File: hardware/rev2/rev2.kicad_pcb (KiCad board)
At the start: 4 copper layers, 60 x 40 mm, 109 parts, among them J1 USB_C_Receptacle_USB2.0_16P, J2 uFL, J3 uFL, J4 Antenna RF and GNSS Data, J5 Antenna GND, J6 uFL, Q1 SS8050, SW1 SW_Push, SW2 SW_Push, U1 EClamp2522P, U2 ESP32-S3FN8, U3 SX1262IMLTRT, U4 PE4259, U5 MP2664GG-xxxx-P, U6 MAX17055ETB+, U7 TPS63805YFFR, Y1 ECS-2520SMV-400-FN-TR, Y2 TXO-20CSMV-320

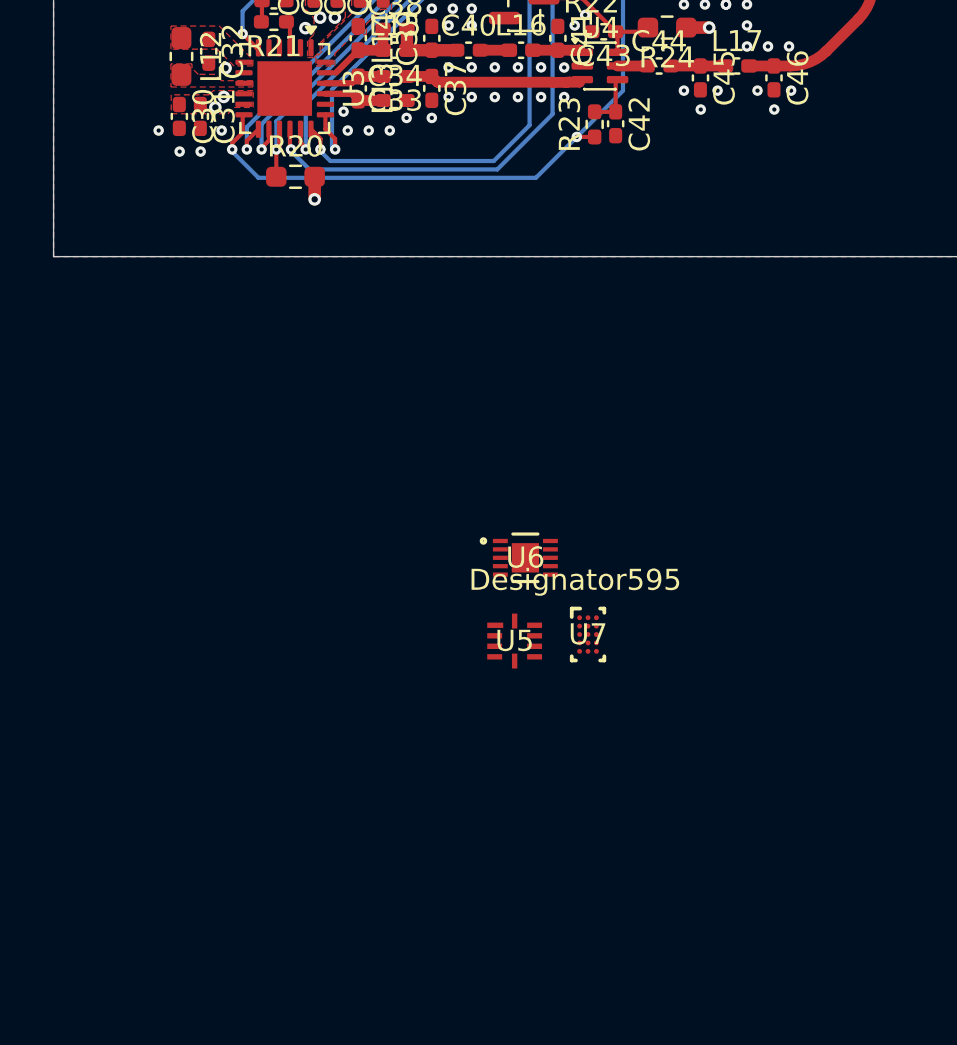
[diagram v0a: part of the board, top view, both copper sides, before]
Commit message: Started power system layout
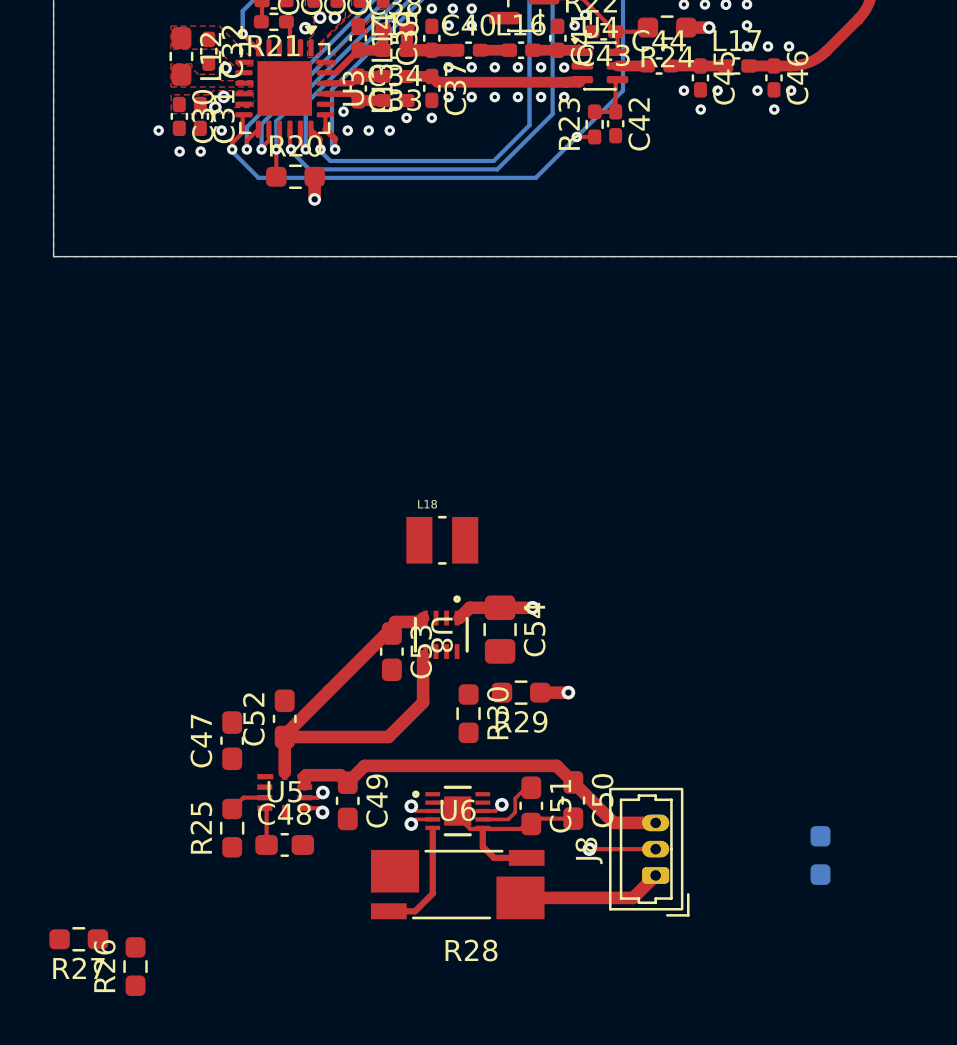
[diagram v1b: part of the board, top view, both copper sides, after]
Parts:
- removed U7: TPS63805YFFR, _footprints:YFF0015AHAN
- added C47: 1µF, Capacitor_SMD:C_0603_1608Metric_Pad1.08x0.95mm_HandSolder, F.Cu at (136.5, 120.0)
- added C48: 100nF, Capacitor_SMD:C_0603_1608Metric_Pad1.08x0.95mm_HandSolder, F.Cu at (139.0, 125.0)
- added C49: 4.7µF, Capacitor_SMD:C_0603_1608Metric_Pad1.08x0.95mm_HandSolder, F.Cu at (142.0, 122.9)
- added C50: 0.1µF, Capacitor_SMD:C_0603_1608Metric_Pad1.08x0.95mm_HandSolder, F.Cu at (152.7, 122.9)
- added C51: 0.47µF, Capacitor_SMD:C_0603_1608Metric_Pad1.08x0.95mm_HandSolder, F.Cu at (150.7, 123.1)
- added C52: 10µF, Capacitor_SMD:C_0603_1608Metric_Pad1.08x0.95mm_HandSolder, F.Cu at (139.0, 119.0)
- added C53: 22µF, Capacitor_SMD:C_0603_1608Metric_Pad1.08x0.95mm_HandSolder, F.Cu at (144.1, 115.8)
- added C54: 47µF, Capacitor_SMD:C_0805_2012Metric_Pad1.18x1.45mm_HandSolder, F.Cu at (149.2, 114.8)
- added J8: Battery Connection, Connector_Molex:Molex_PicoBlade_53047-0310_1x03_P1.25mm_Vertical, F.Cu at (156.7, 126.5)
- added L18: 1µH, _footprints:INDC2520X120N, F.Cu at (146.5, 110.5)
- added R25: 300kΩ, Resistor_SMD:R_0603_1608Metric_Pad0.98x0.95mm_HandSolder, F.Cu at (136.5, 124.2)
- added R26: TBD, Resistor_SMD:R_0603_1608Metric_Pad0.98x0.95mm_HandSolder, F.Cu at (131.9, 130.8)
- added R27: TBD, Resistor_SMD:R_0603_1608Metric_Pad0.98x0.95mm_HandSolder, F.Cu at (129.2, 129.5)
- added R28: 0.01Ω, _footprints:RES_WSK2512R0100FEA, F.Cu at (147.2, 126.9)
- added R29: 511kΩ, Resistor_SMD:R_0603_1608Metric_Pad0.98x0.95mm_HandSolder, F.Cu at (150.2, 117.8)
- added R30: 91kΩ, Resistor_SMD:R_0603_1608Metric_Pad0.98x0.95mm_HandSolder, F.Cu at (147.8, 118.8)
- added R31: TBD, Resistor_SMD:R_0603_1608Metric_Pad0.98x0.95mm_HandSolder, B.Cu at (164.5, 125.5)
- added U8: TPS631000DRLR, _footprints:TPS631000DRLR_TEX, F.Cu at (146.5, 115.0)
- moved U5 13.1 mm to (139.0, 122.5)
- moved U6 12.5 mm to (147.2, 123.4)
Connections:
- net /Power/BATT- renamed /Power/CSP
- U6 pad 5: GND -> /Power/CSN
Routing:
- net Net-(U5-SYS): track 0.00 -> 20.2 mm
- net /Power/BATT+: track 0.00 -> 18.7 mm
- net /Power/CSP: track 0.00 -> 10.7 mm
- net /Power/BATT-: track 0.00 -> 6.88 mm
- net /Power/CSN: track 0.00 -> 5.52 mm
- net +3.3V: track 0.00 -> 5.02 mm, vias 0 -> 2
- net Net-(U6-REG): track 0.00 -> 3.43 mm
- net /Power/NTC: track 0.00 -> 3.16 mm, vias 0 -> 1
- net /RXD/SDA: track 16.8 -> 18.9 mm, vias 1 -> 3
- net /TXD/SCL: track 20.2 -> 22.2 mm, vias 1 -> 3
- net /Power/VDD: track 0.00 -> 1.79 mm
- net /Power/INT: track 0.50 -> 2.27 mm
- net /ESP32/ALRT: track 0.85 -> 1.88 mm, vias 1 -> 2

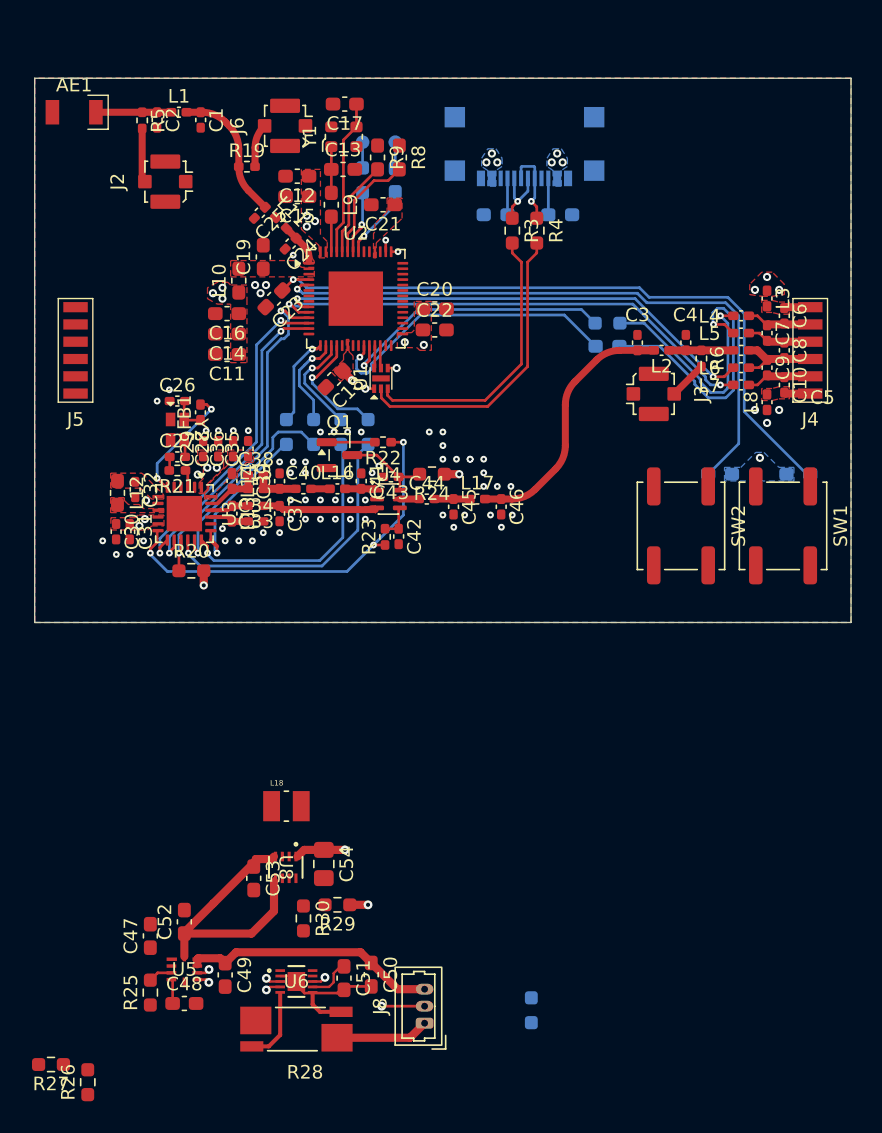
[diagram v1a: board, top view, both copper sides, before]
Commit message: added testpoints, added LEDs, fixed a lot of DRC stuff
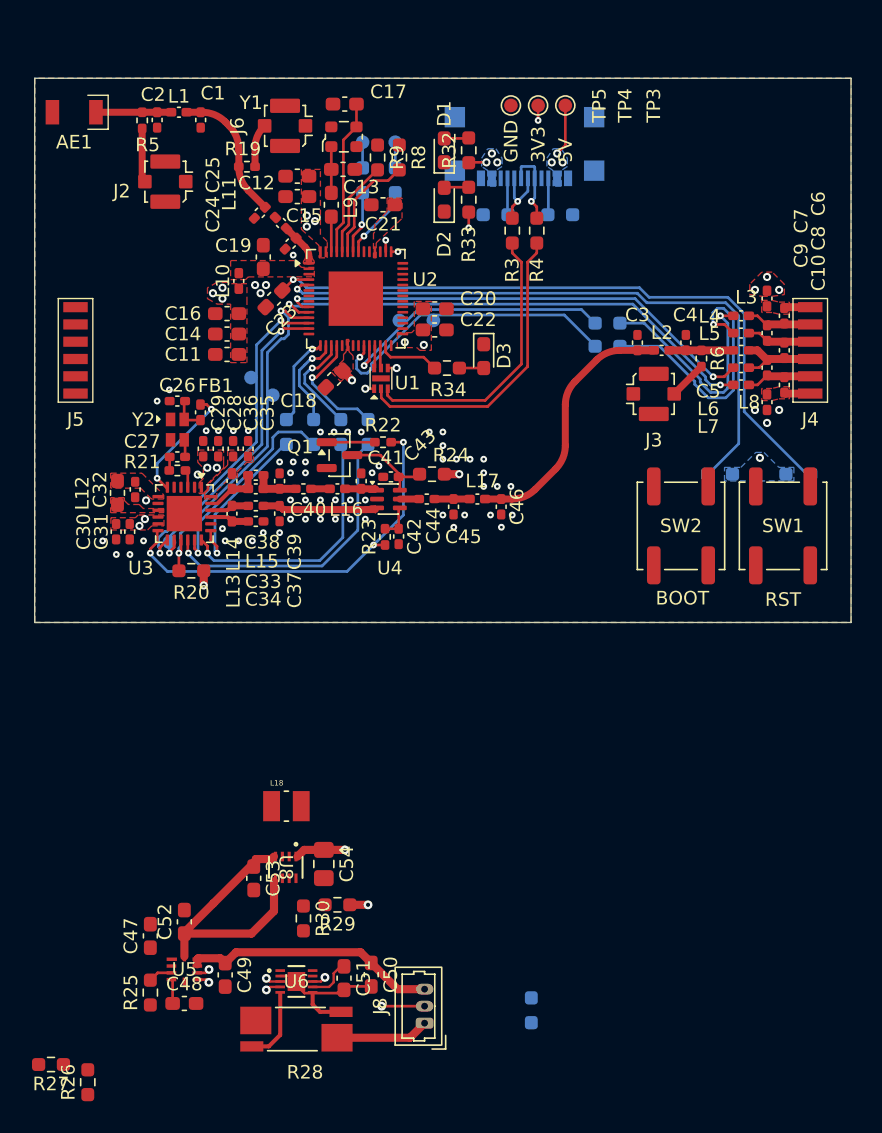
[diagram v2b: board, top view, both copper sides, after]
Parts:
- added D1: LED, LED_SMD:LED_0603_1608Metric_Pad1.05x0.95mm_HandSolder, F.Cu at (158.1, 62.3)
- added D2: LED, LED_SMD:LED_0603_1608Metric_Pad1.05x0.95mm_HandSolder, F.Cu at (158.1, 65.9)
- added D3: LED, LED_SMD:LED_0603_1608Metric_Pad1.05x0.95mm_HandSolder, F.Cu at (161.0, 77.4)
- added R32: 110 R, Resistor_SMD:R_0603_1608Metric_Pad0.98x0.95mm_HandSolder, F.Cu at (159.9, 62.3)
- added R33: 27 R, Resistor_SMD:R_0603_1608Metric_Pad0.98x0.95mm_HandSolder, F.Cu at (159.9, 65.9)
- added R34: 27 R, Resistor_SMD:R_0603_1608Metric_Pad0.98x0.95mm_HandSolder, F.Cu at (158.3, 78.3)
- added TP10: TestPoint, TestPoint:TestPoint_Pad_D1.0mm, B.Cu at (145.5, 80.3)
- added TP11: TestPoint, TestPoint:TestPoint_Pad_D1.0mm, B.Cu at (143.9, 79.0)
- added TP12: TestPoint, TestPoint:TestPoint_Pad_D1.0mm, B.Cu at (137.9, 91.1)
- added TP3: TestPoint, TestPoint:TestPoint_Pad_D1.0mm, F.Cu at (167.0, 59.0)
- added TP4: TestPoint, TestPoint:TestPoint_Pad_D1.0mm, F.Cu at (165.0, 59.0)
- added TP5: TestPoint, TestPoint:TestPoint_Pad_D1.0mm, F.Cu at (163.0, 59.0)
- added TP7: TestPoint, TestPoint:TestPoint_Pad_D1.0mm, B.Cu at (157.3, 74.8)
- added TP8: TestPoint, TestPoint:TestPoint_Pad_D1.0mm, B.Cu at (154.8, 74.8)
- C47: value 1µF -> 1 uF
- C48: value 100nF -> 100 nF
- C49: value 4.7µF -> 4.7 uF
- C5: value DC-Block -> 100 pF
- C50: value 0.1µF -> 0.1 uF
- C51: value 0.47µF -> 0.47 uF
- C52: value 10µF -> 10 uF
- C53: value 22µF -> 22 uF
- C54: value 47µF -> 47 uF
- L10: footprint Inductor_SMD:L_0603_1608Metric_Pad1.05x0.95mm_HandSolder -> Inductor_SMD:L_0402_1005Metric_Pad0.77x0.64mm_HandSolder
- L18: value 1µH -> 1 uH
- R1, R2: value 5.1k -> 5.1 k; footprint Inductor_SMD:L_0603_1608Metric_Pad1.05x0.95mm_HandSolder -> Resistor_SMD:R_0603_1608Metric_Pad0.98x0.95mm_HandSolder
- R10, R7, R8, R9: value 10k -> 10 k; footprint Inductor_SMD:L_0603_1608Metric_Pad1.05x0.95mm_HandSolder -> Resistor_SMD:R_0603_1608Metric_Pad0.98x0.95mm_HandSolder
- R15, R17: footprint Inductor_SMD:L_0603_1608Metric_Pad1.05x0.95mm_HandSolder -> Resistor_SMD:R_0603_1608Metric_Pad0.98x0.95mm_HandSolder
- R20, R24: value 10k -> 10 k
- R25: value 300kΩ -> 300 k
- R28: value 0.01Ω -> 0.01 R
- R29: value 511kΩ -> 511 k
- R30: value 91kΩ -> 91 k
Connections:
- U2 pad 27: unconnected-(U2-GPIO21-Pad27) -> /ESP32/STATUS_LED
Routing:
- net +5V: track 22.2 -> 27.2 mm
- net /ESP32/STATUS_LED: track 0.00 -> 4.56 mm
- net +3V3: track 3.82 -> 6.08 mm, vias 20 -> 22
- net Net-(D2-A): track 0.00 -> 1.82 mm
- net Net-(D1-A): track 0.00 -> 1.80 mm
- net Net-(D3-A): track 0.00 -> 1.79 mm
- net GND: vias 66 -> 65
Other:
- board text added: "3V3"
- board text added: "5V"
- board text added: "BOOT"
- board text added: "GND"
- board text added: "RST"

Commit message: Finished power layout
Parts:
- added JP1: Storage mode jumper, Connector_PinHeader_1.00mm:PinHeader_1x03_P1.00mm_Vertical, F.Cu at (166.9, 68.9)
- added R35: TBD, Resistor_SMD:R_0603_1608Metric_Pad0.98x0.95mm_HandSolder, F.Cu at (168.8, 71.2)
- R26, R27, R29, R30: moved to B.Cu
- R28: footprint _footprints:RES_WSK2512R0100FEA -> _footprints:RES_WSK1206R0100FEA
- moved R26 72.8 mm to (169.9, 68.7), turned to -90 degrees
- moved R27 71.4 mm to (168.4, 69.8), turned to -90 degrees
- moved C53 67.8 mm to (181.3, 59.1), turned to 180 degrees
- moved C49 67.4 mm to (174.5, 63.9)
- moved C48 67.4 mm to (171.5, 66.0)
- moved U5 67.4 mm to (171.5, 63.5)
- moved C52 67.2 mm to (171.5, 60.1)
- moved C47 66.9 mm to (168.6, 61.4)
- moved R30 65.5 mm to (178.4, 60.9), turned to 180 degrees
- moved R25 65.2 mm to (168.8, 67.6), turned to -90 degrees
- moved U8 64.1 mm to (181.5, 61.4), turned to 180 degrees
- moved J8 63.4 mm to (185.4, 70.0)
- moved R28 63.1 mm to (175.7, 70.6)
- moved L18 62.8 mm to (185.7, 61.4), turned to -90 degrees
- moved C51 62.2 mm to (179.2, 67.8)
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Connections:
- C54 pad 1: +3.3V -> +3V3
- R25 pad 2: /Power/INT -> Net-(JP1-A)
- R29 pad 1: +3.3V -> +3V3
- R31 pad 1: +3.3V -> +3V3
- U8 pad 1: +3.3V -> +3V3
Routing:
- net /Power/NTC: track 3.16 -> 30.8 mm, vias 1 -> 2
- net /ESP32/ALRT: track 1.88 -> 28.7 mm
- net /Power/INT: track 2.27 -> 21.5 mm, vias 1 -> 0
- net /TXD/SCL: track 22.2 -> 38.9 mm, vias 3 -> 5
- net /RXD/SDA: track 18.9 -> 35.2 mm, vias 3 -> 5
- net +3V3: track 6.08 -> 14.7 mm, vias 22 -> 26
- net +3.3V: track 5.02 -> 0.00 mm, vias 2 -> 0
- net +5V: track 27.2 -> 31.7 mm
- net /Power/VDD: track 1.79 -> 5.67 mm, vias 0 -> 1
- net Net-(U8-LX2): track 0.00 -> 3.79 mm
- net Net-(U8-LX1): track 0.00 -> 3.76 mm
- net Net-(U8-FB): track 0.00 -> 3.62 mm, vias 0 -> 1
- net GND: track 0.00 -> 2.54 mm, vias 65 -> 90
- net /Power/CSN: track 5.52 -> 3.10 mm
- net Net-(U5-SYS): track 20.2 -> 22.5 mm
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
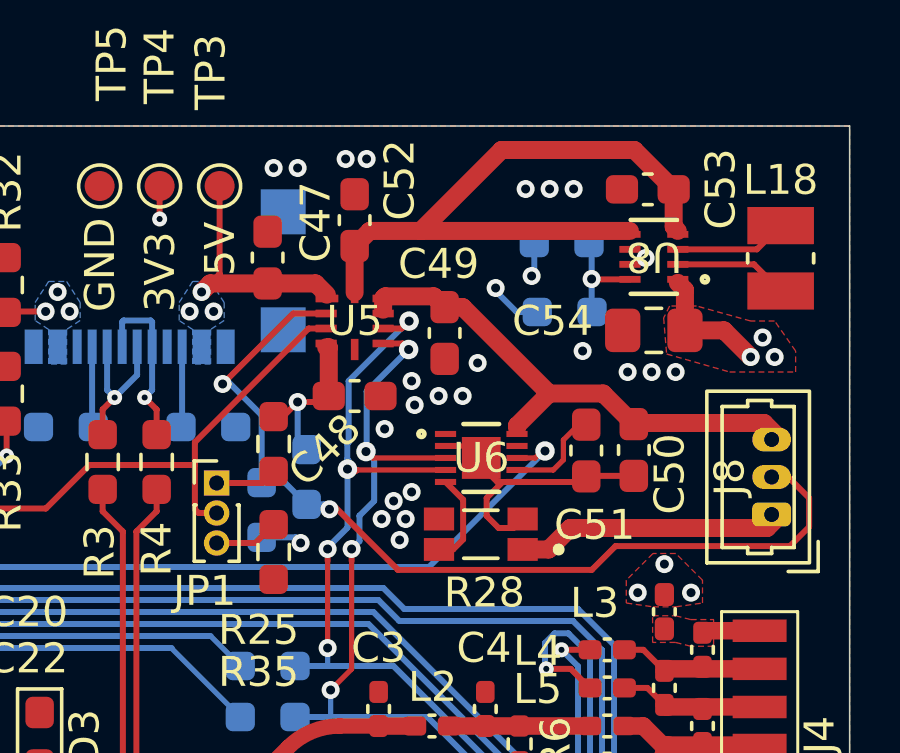
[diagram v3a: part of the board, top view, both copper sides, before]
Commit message: Rerouted i2c in power layout to avoid noisy ground
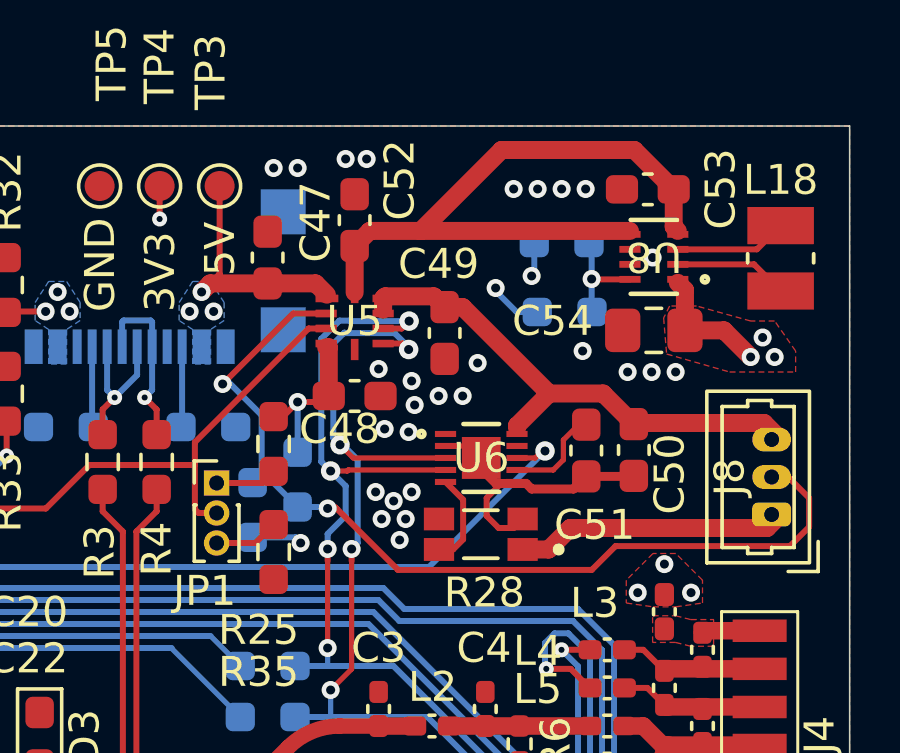
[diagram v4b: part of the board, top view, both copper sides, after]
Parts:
- moved R26 0.31 mm to (169.6, 68.8)
- moved R27 0.30 mm to (168.1, 69.8)
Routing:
- net /TXD/SCL: track 38.9 -> 42.4 mm
- net /RXD/SDA: track 35.2 -> 37.8 mm
- net /Power/NTC: track 30.8 -> 31.4 mm
- net GND: track 2.54 -> 2.53 mm, vias 90 -> 94
